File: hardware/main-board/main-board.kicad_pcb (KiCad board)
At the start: 4 copper layers, 105 x 38 mm, 96 parts, among them J1 USB_C_Receptacle_USB2.0, J2 DNI, J3 Display Connector, J4 Conn_01x02, SW1 SW_Push, SW2 SW_Push, SW3 SW_Push, SW4 SW_Push, SW5 SW_Detect, SW6 SW_Boot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

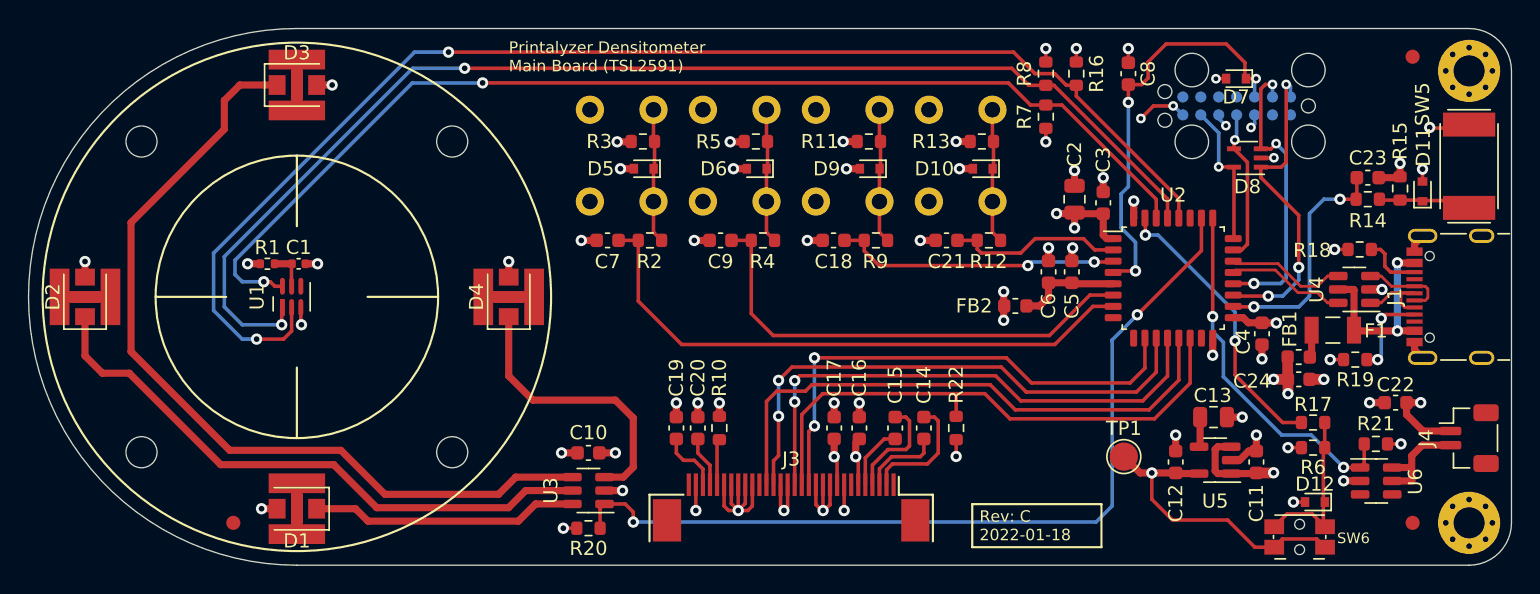
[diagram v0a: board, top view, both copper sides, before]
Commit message: Merge hardware from spectrodensitometer project and rename
The spectrodensitometer R&D project is going to be used as the hardware
baseline, rather than the original DPD-100, because it has various
changes that will be useful to this project. Those changes include
different LEDs, different LED drivers, a temperature sensor, and a 1.8V
capable LDO.
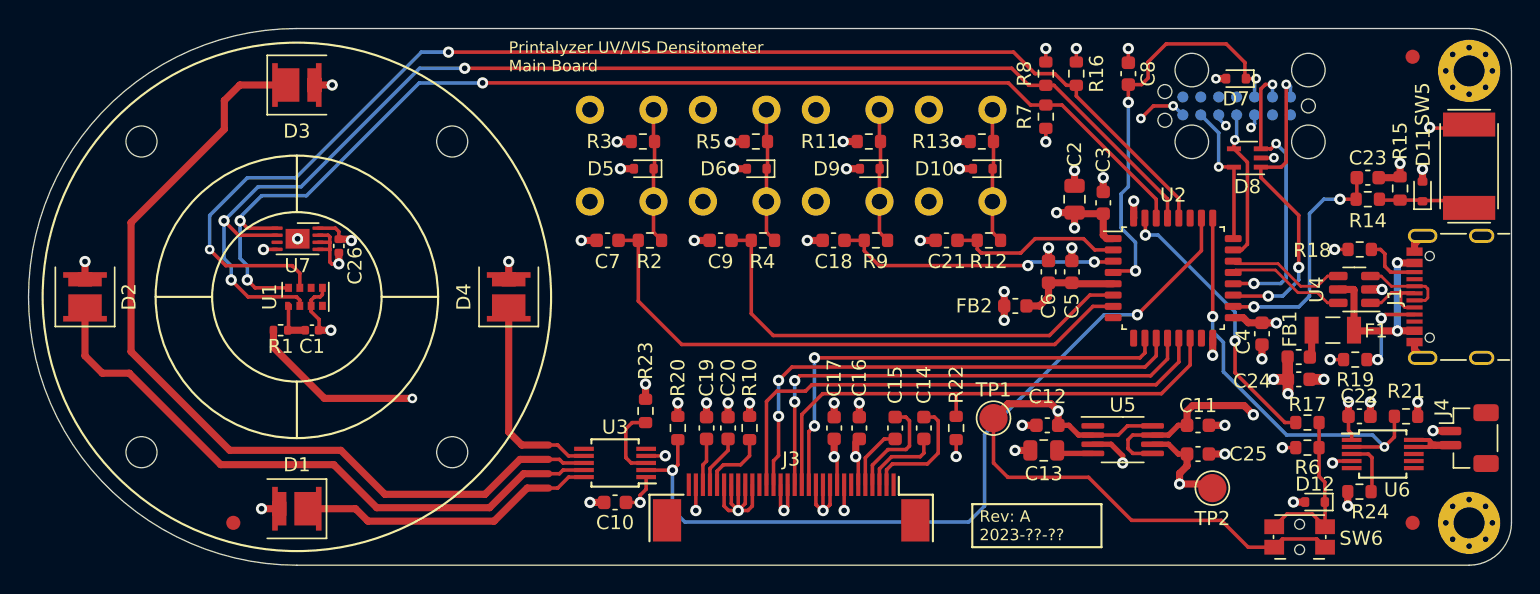
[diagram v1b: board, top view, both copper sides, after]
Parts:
- removed G2: LOGO, lib_fp:densitometer-logo-16_9mm
- added C25: 1uF, Capacitor_SMD:C_0603_1608Metric, F.Cu at (123.8, 71.1)
- added C26: 1uF, Capacitor_SMD:C_0402_1005Metric, F.Cu at (63.0, 56.4)
- added R23: 16.5k, Resistor_SMD:R_0603_1608Metric, F.Cu at (84.7, 68.1)
- added R24: 16.5k, Resistor_SMD:R_0603_1608Metric, F.Cu at (135.2, 73.8)
- added TP2: 1.8V, TestPoint:TestPoint_Pad_D2.0mm, F.Cu at (124.8, 73.5)
- added U7: MCP9808, Package_DFN_QFN:DFN-8-1EP_3x2mm_P0.5mm_EP1.7x1.4mm, F.Cu at (60.0, 55.9)
- C10, C22: value 0.1uF -> 2.2uF
- C13: value 22nF -> 10nF
- D1, D2, D3, D4: footprint lib_fp:LED_WL-SWTP-3022-1MP -> lib_fp:SunLike_LED_S1S0
- D10, D11, D12, D5, D6, D7, D9: value uClamp0501H -> uClamp3301H
- F1: value 250mA -> 500mA
- R20, R21: value 10K -> 200K
- REF1, REF2, REF4, REF5, REF6: footprint kikit:Tab -> PCM_kikit:Tab
- U1: value TSL2591 -> AS7343; footprint lib_fp:AMS_TSL2591 -> lib_fp:AMS_OLGA-8_2.0x3.1mm_P0.8mm
- U3, U6: value AP2502 -> MIC4811; footprint Package_TO_SOT_SMD:SOT-23-6 -> Package_SO:MSOP-10_3x3mm_P0.5mm
- U5: value RT9193 -> TC1301A-APA; footprint Package_TO_SOT_SMD:SOT-23-5 -> Package_SO:MSOP-8_3x3mm_P0.65mm
- moved C13 12.3 mm to (112.9, 70.9), turned to 0 degrees
- moved TP1 9.62 mm to (109.3, 68.6)
- moved R20 9.51 mm to (87.0, 69.3), turned to 90 degrees
- moved C12 9.45 mm to (113.1, 69.1), turned to 0 degrees
- moved U5 6.71 mm to (118.5, 70.1), turned to 0 degrees
- moved C11 4.88 mm to (123.8, 69.1), turned to 180 degrees
- moved C1 4.80 mm to (61.1, 62.4)
- moved R1 4.80 mm to (58.9, 62.4)
- moved C10 3.98 mm to (82.5, 74.6), turned to 180 degrees
- moved R21 2.89 mm to (138.5, 68.5)
- moved C22 2.74 mm to (135.2, 68.5), turned to 0 degrees
- moved U3 2.71 mm to (82.5, 71.8)
- moved C19 2.14 mm to (89.0, 69.3)
- moved C20 2.14 mm to (90.5, 69.3)
- moved R10 2.14 mm to (92.1, 69.3)
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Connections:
- R1 pad 1: +3.3V -> +1V8
- R16 pad 2: /TSL_INT -> /AS_INT
- U1 pad 1: /I2C1_SCL -> Net-(C1-Pad1)
- U1 pad 2: /TSL_INT -> /I2C1_SCL
- U1 pad 5: Net-(C1-Pad1) -> GND
- U1 pad 6: /I2C1_SDA -> unconnected-(U1-Pad6)
- U2 pad 28: /TSL_INT -> /AS_INT
- U3 pad 1: /RLED_EN -> +5V
- U3 pad 2: GND -> /RLED_EN
- U3 pad 3: Net-(D4-Pad1) -> Net-(R23-Pad1)
- U3 pad 4: Net-(D3-Pad1) -> GND
- U3 pad 5: Net-(D2-Pad1) -> unconnected-(U3-Pad5)
- U3 pad 6: Net-(D1-Pad1) -> unconnected-(U3-Pad6)
- U5 pad 1: +5V -> unconnected-(U5-Pad1)
- U5 pad 2: GND -> +3.3V
- U5 pad 3: +5V -> GND
- U5 pad 5: +3.3V -> +5V
- U6 pad 1: /TLED_EN -> +5V
- U6 pad 2: GND -> /TLED_EN
- U6 pad 3: unconnected-(U6-Pad3) -> Net-(R24-Pad1)
- U6 pad 4: unconnected-(U6-Pad4) -> GND
- U6 pad 5: Net-(J4-Pad2) -> unconnected-(U6-Pad5)
- U6 pad 6: Net-(J4-Pad2) -> unconnected-(U6-Pad6)
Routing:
- net +1V8: track 0.00 -> 101.6 mm, vias 0 -> 2
- net /TSL_INT: track 92.7 -> 0.00 mm, vias 2 -> 0
- net /AS_INT: track 0.00 -> 90.1 mm, vias 0 -> 2
- net +3.3V: track 48.5 -> 71.5 mm
- net GND: track 83.4 -> 96.9 mm, vias 55 -> 61
- net +5V: track 21.5 -> 28.2 mm, vias 9 -> 10
- net Net-(D4-Pad1): track 20.1 -> 14.2 mm
- net Net-(R23-Pad1): track 0.00 -> 5.21 mm
- net /I2C1_SDA: track 79.9 -> 84.2 mm, vias 2 -> 3
- net /RLED_EN: track 62.2 -> 58.0 mm
- net /I2C1_SCL: track 86.9 -> 90.9 mm, vias 2 -> 3
- net Net-(R24-Pad1): track 0.00 -> 3.98 mm
- net /TLED_EN: track 25.7 -> 29.6 mm
- net /DISP_~{RES}: track 39.7 -> 37.4 mm
- net /DISP_MOSI: track 40.2 -> 37.9 mm
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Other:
- board text added: "Printalyzer UV/VIS Densitometer Main Board"
- board text added: "UV/VIS Densitometer Main Board"
- board text removed: "Printalyzer Densitometer Main Board (TSL2591)"

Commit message: Finished first pass at layout for new design changes
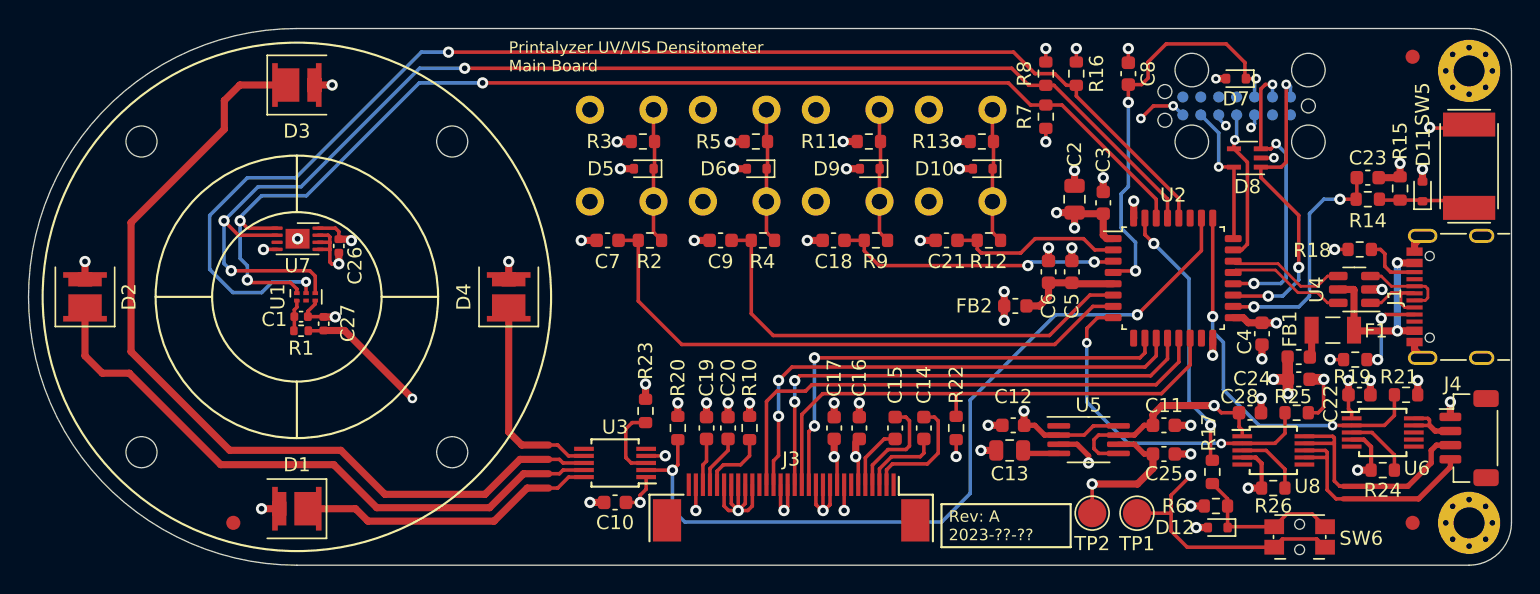
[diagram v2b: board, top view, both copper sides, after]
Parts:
- added C27: 4.7uF, Capacitor_SMD:C_0402_1005Metric, F.Cu at (61.9, 61.9)
- added C28: 2.2uF, Capacitor_SMD:C_0603_1608Metric, F.Cu at (127.5, 68.2)
- added R25: 200K, Resistor_SMD:R_0603_1608Metric, F.Cu at (130.8, 68.2)
- added R26: 16.5k, Resistor_SMD:R_0603_1608Metric, F.Cu at (129.1, 73.5)
- added U8: MIC4811, Package_SO:MSOP-10_3x3mm_P0.5mm, F.Cu at (129.1, 70.9)
- D10, D11, D12, D5, D6, D7, D9: value uClamp3301H -> uClamp0501H
- J4: value Conn_01x02 -> Conn_01x04; footprint Connector_JST:JST_SH_BM02B-SRSS-TB_1x02-1MP_P1.00mm_Vertical -> Connector_JST:JST_SH_BM04B-SRSS-TB_1x04-1MP_P1.00mm_Vertical
- U1: value AS7343 -> TSL2585; footprint lib_fp:AMS_OLGA-8_2.0x3.1mm_P0.8mm -> lib_fp:AMS_TSL2585_OLGA-6_2x1mm_P0.65mm
- moved TP1 12.2 mm to (119.5, 75.3), turned to 180 degrees
- moved TP2 8.69 mm to (116.3, 75.3)
- moved R6 7.68 mm to (125.1, 74.8)
- moved R17 7.59 mm to (124.8, 72.4), turned to 90 degrees
- moved D12 7.12 mm to (125.2, 76.3)
- moved C13 2.41 mm to (110.5, 70.9)
- moved C11 2.41 mm to (121.4, 69.1)
- moved C12 2.41 mm to (110.7, 69.1)
- moved C25 2.41 mm to (121.4, 71.1)
- moved U5 2.41 mm to (116.1, 70.1)
- moved R24 2.25 mm to (136.9, 72.3)
- moved C22 1.52 mm to (135.2, 66.9)
- moved R21 1.52 mm to (138.5, 66.9)
- moved U6 1.52 mm to (136.9, 69.6)
- moved R1 1.45 mm to (60.3, 62.4)
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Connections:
- net /TLED_EN renamed /TVLED_EN
- net Net-(J4-Pad2) renamed /VIS_LED_C
- C1 pad 1: Net-(C1-Pad1) -> Net-(U1-VDD)
- R1 pad 1: +1V8 -> Net-(U1-VDD)
- R1 pad 2: Net-(C1-Pad1) -> +1V8
- R16 pad 2: /AS_INT -> /TSL_INT
- U1 pad 1: Net-(C1-Pad1) -> Net-(U1-VDD)
- U1 pad 2: /I2C1_SCL -> unconnected-(U1-VSYNC/GPIO-Pad2)
- U1 pad 4: unconnected-(U1-Pad4) -> /I2C1_SCL
- U1 pad 5: GND -> /TSL_INT
- U1 pad 6: unconnected-(U1-Pad6) -> /I2C1_SDA
- U2 pad 28: /AS_INT -> /TSL_INT
- U2 pad 8: unconnected-(U2-Pad8) -> /TULED_EN
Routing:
- net /TSL_INT: track 0.00 -> 92.0 mm, vias 0 -> 2
- net /AS_INT: track 90.1 -> 0.00 mm, vias 2 -> 0
- net /TULED_EN: track 0.00 -> 24.4 mm, vias 0 -> 2
- net /UV_LED1_C: track 0.00 -> 17.4 mm
- net +3.3V: track 71.5 -> 54.9 mm, vias 14 -> 15
- net /UV_LED2_C: track 0.00 -> 16.4 mm
- net GND: track 96.9 -> 105.0 mm, vias 61 -> 62
- net +1V8: track 101.6 -> 95.2 mm
- net Net-(U8-RSET): track 0.00 -> 4.91 mm
- net /VIS_LED_C: track 8.34 -> 4.30 mm
- net Net-(C1-Pad1): track 2.94 -> 0.00 mm
- net +5V: track 28.2 -> 31.0 mm
- net Net-(U1-VDD): track 0.00 -> 2.22 mm
- net /TVLED_EN: track 29.6 -> 27.4 mm
- net Net-(D11-IO1): track 6.60 -> 4.57 mm
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
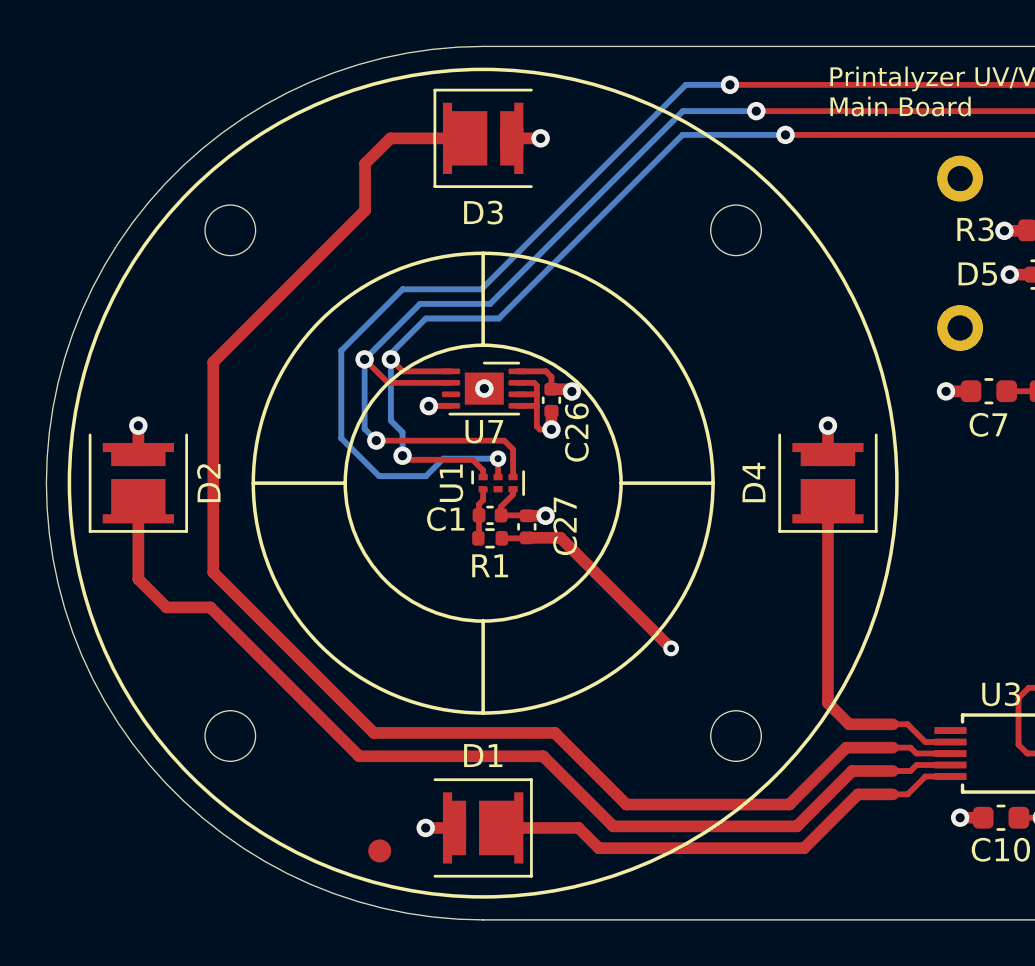
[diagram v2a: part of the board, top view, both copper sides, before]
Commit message: Clean up thermal zones around LED footprints
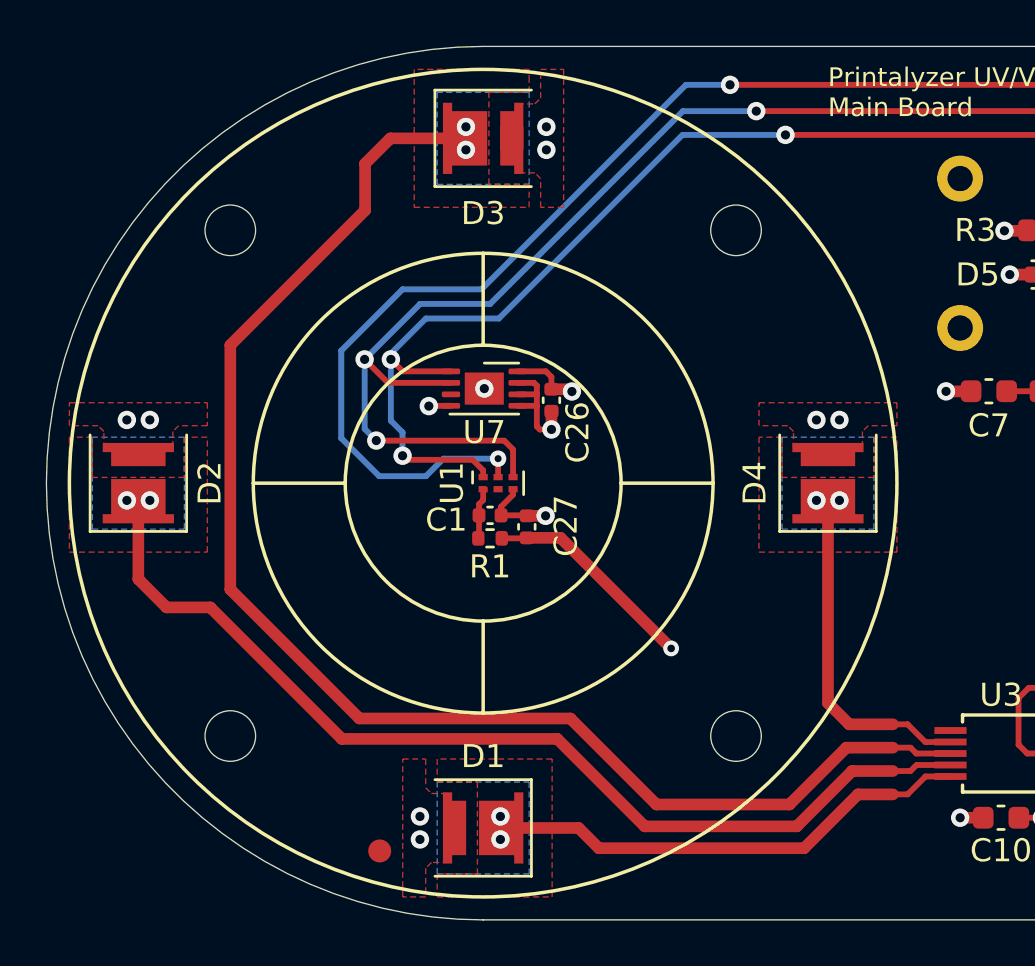
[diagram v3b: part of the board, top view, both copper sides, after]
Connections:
- net Net-(D1-K) renamed /RLED1
- net Net-(D2-K) renamed /RLED2
- net Net-(D3-K) renamed /RLED3
- net Net-(D4-K) renamed /RLED4
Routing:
- net +5V: track 31.0 -> 26.6 mm, vias 10 -> 14
- net /RLED3: track 62.1 -> 61.5 mm, vias 0 -> 2
- net /RLED4: vias 0 -> 2
- net /RLED2: vias 0 -> 2
- net /RLED1: vias 0 -> 2
- added copper zone on F.Cu, net +5V
- added copper zone on B.Cu, net /RLED1
- added copper zone on F.Cu, net /RLED1
- added copper zone on B.Cu, net /RLED2
- added copper zone on F.Cu, net /RLED2
- added copper zone on B.Cu, net /RLED3
- added copper zone on F.Cu, net /RLED3
- added copper zone on B.Cu, net /RLED4
- added copper zone on F.Cu, net /RLED4
